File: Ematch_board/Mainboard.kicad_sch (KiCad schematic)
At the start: 72 parts, among them J10 Conn_01x02_Male, J7 Conn_01x06_Female, J8 USB_C_Receptacle_USB2.0, J9 Conn_01x02_Male, Q1 MMDT2222A, Q2 MMDT2222A, U2 LTC4411, U3 RT9025-25GSP, U4 LTC4411, U5 SN65HVD230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

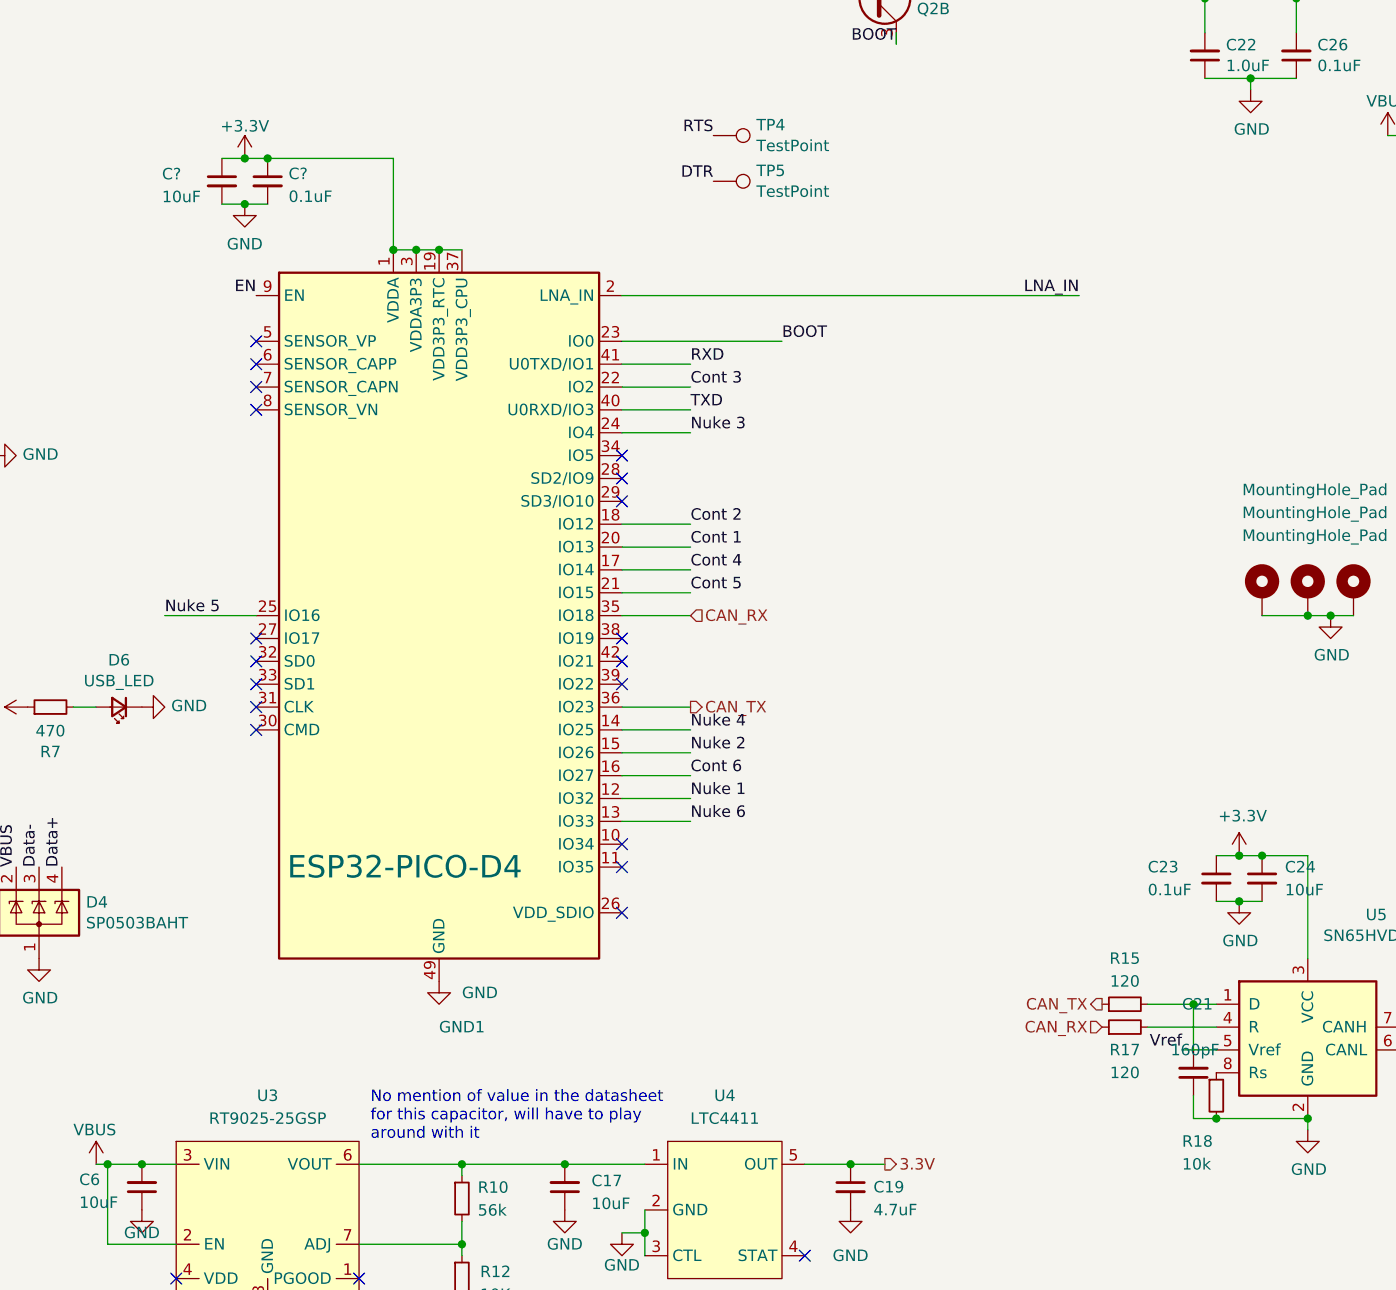
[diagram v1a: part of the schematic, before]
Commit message: removed ground traces
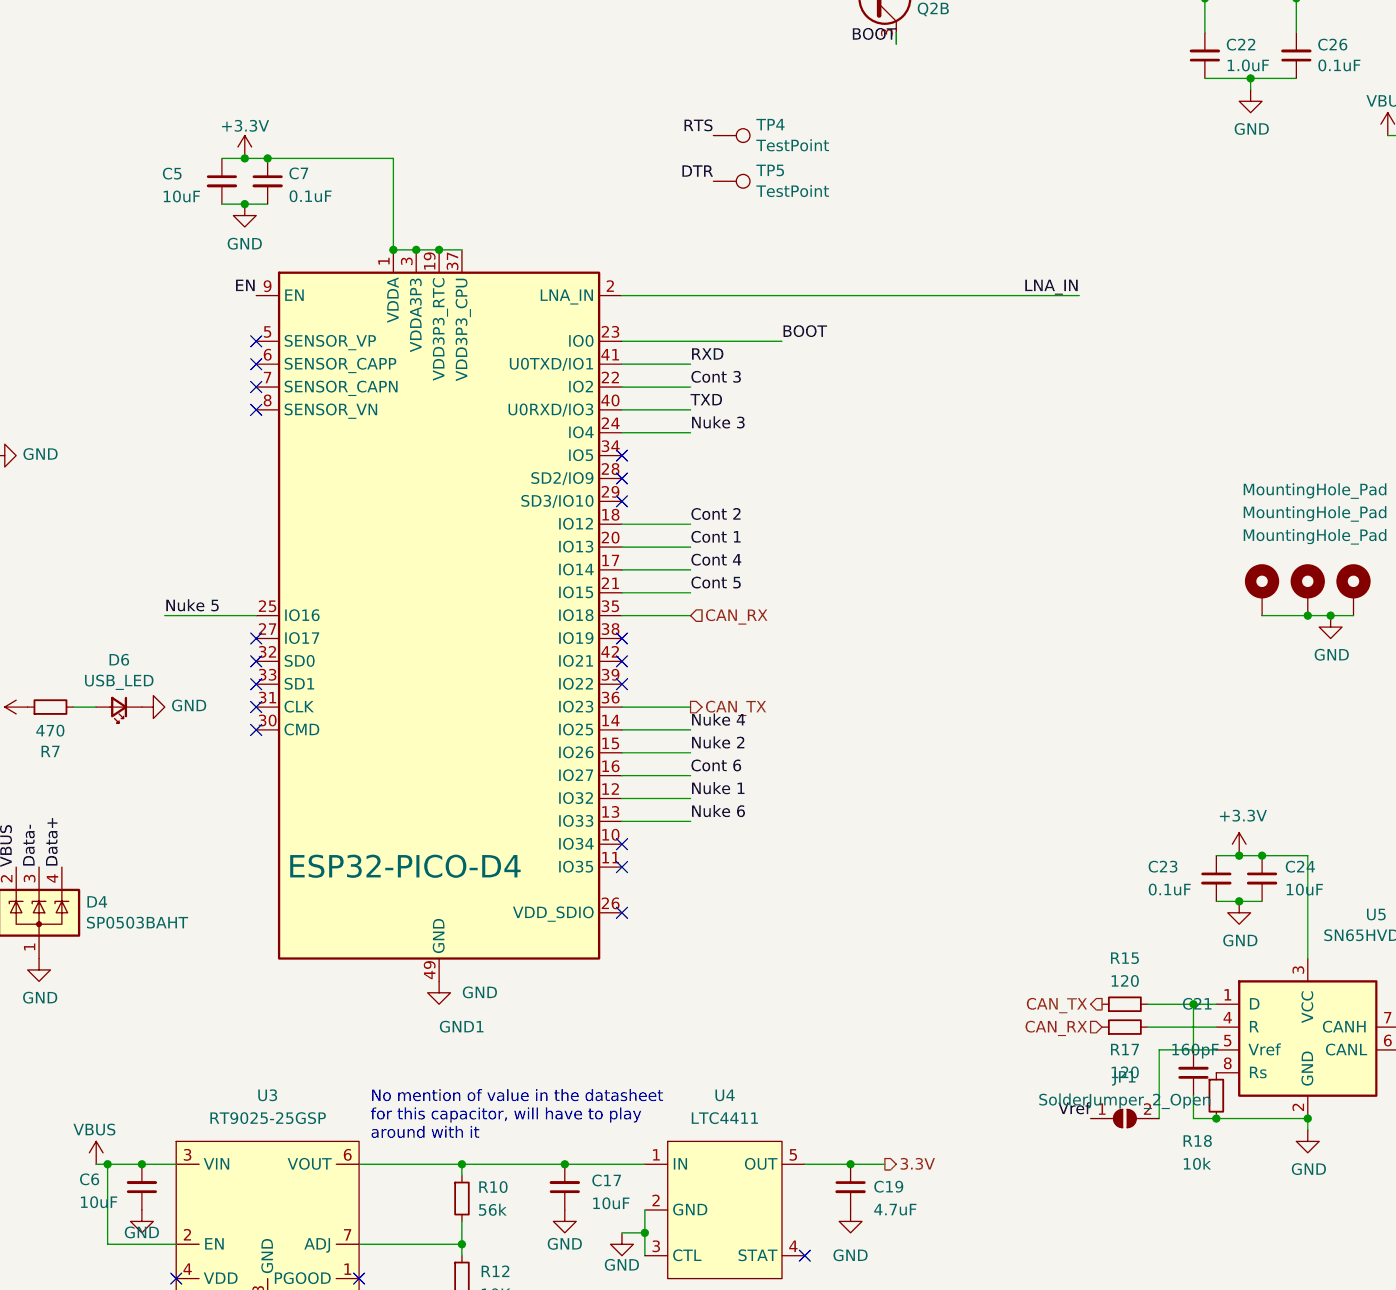
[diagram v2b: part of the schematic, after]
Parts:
- added JP1: SolderJumper_2_Open, Jumper:SolderJumper-2_P1.3mm_Open_RoundedPad1.0x1.5mm, symbol Jumper:SolderJumper_2_Open
- C5, C7: renamed from C?; footprint (none) -> Capacitor_SMD:C_0603_1608Metric
- TP1, TP2, TP3, TP4, TP5: footprint TestPoint:TestPoint_THTPad_1.0x1.0mm_Drill0.5mm -> TestPoint:TestPoint_Pad_D1.0mm
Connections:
- net Vref: now also JP1.1 (A); no longer U5.5 (Vref)
- new net: JP1.2 (B), U5.5 (Vref)
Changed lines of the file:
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@@
     (stroke (width 0) (type default) (color 0 0 0 0))
   )
-  (wire (pts (xy 186.69 154.94) (xy 190.5 154.94))
+  (wire (pts (xy 184.15 154.94) (xy 190.5 154.94))
     (stroke (width 0) (type default) (color 0 0 0 0))
   )
@@
   )
   (wire (pts (xy -12.7 91.44) (xy -5.08 91.44))
+    (stroke (width 0) (type default) (color 0 0 0 0))
+  )
+  (wire (pts (xy 184.15 162.56) (xy 184.15 154.94))
     (stroke (width 0) (type default) (color 0 0 0 0))
   )
@@
     (effects (font (size 1.27 1.27)) (justify right bottom))
   )
+  (label "Vref" (at 176.53 162.56 180)
+    (effects (font (size 1.27 1.27)) (justify right bottom))
+  )
   (label "Data-" (at 200.66 33.02 0)
     (effects (font (size 1.27 1.27)) (justify left bottom))
@@
   (label "Cont 5" (at 132.08 104.14 0)
     (effects (font (size 1.27 1.27)) (justify left bottom))
-  )
-  (label "Vref" (at 186.69 154.94 180)
-    (effects (font (size 1.27 1.27)) (justify right bottom))
   )
   (label "Data-" (at 44.45 95.25 0)
@@
       (effects (font (size 1.27 1.27)) (justify left))
     )
-    (property "Footprint" "TestPoint:TestPoint_THTPad_1.0x1.0mm_Drill0.5mm" (id 2) (at 134.62 63.5 0)
+    (property "Footprint" "TestPoint:TestPoint_Pad_D1.0mm" (id 2) (at 134.62 63.5 0)
       (effects (font (size 1.27 1.27)) hide)
     )
@@
       (effects (font (size 1.27 1.27)) (justify left))
     )
-    (property "Footprint" "TestPoint:TestPoint_THTPad_1.0x1.0mm_Drill0.5mm" (id 2) (at -5.08 106.68 0)
+    (property "Footprint" "TestPoint:TestPoint_Pad_D1.0mm" (id 2) (at -5.08 106.68 0)
       (effects (font (size 1.27 1.27)) hide)
     )
@@
       (effects (font (size 1.27 1.27)) (justify left))
     )
-    (property "Footprint" "TestPoint:TestPoint_THTPad_1.0x1.0mm_Drill0.5mm" (id 2) (at -5.08 101.6 0)
+    (property "Footprint" "TestPoint:TestPoint_Pad_D1.0mm" (id 2) (at -5.08 101.6 0)
       (effects (font (size 1.27 1.27)) hide)
     )
@@
   (symbol (lib_id "power:GND") (at 82.55 60.96 0) (unit 1)
     (in_bom yes) (on_board yes) (fields_autoplaced)
-    (property "Reference" "#PWR?" (id 0) (at 82.55 67.31 0)
+    (property "Reference" "#PWR0114" (id 0) (at 82.55 67.31 0)
       (effects (font (size 1.27 1.27)) hide)
     )
@@
     (pin "2")
   )
+  (symbol (lib_id "Jumper:SolderJumper_2_Open") (at 180.34 162.56 0) (unit 1)
+    (in_bom yes) (on_board yes) (fields_autoplaced)
+    (property "Reference" "JP1" (id 0) (at 180.34 157.9712 0))
+    (property "Value" "SolderJumper_2_Open" (id 1) (at 180.34 160.5081 0))
+    (property "Footprint" "Jumper:SolderJumper-2_P1.3mm_Open_RoundedPad1.0x1.5mm" (id 2) (at 180.34 162.56 0)
+      (effects (font (size 1.27 1.27)) hide)
+    )
+    (property "Datasheet" "~" (id 3) (at 180.34 162.56 0)
+      (effects (font (size 1.27 1.27)) hide)
+    )
+    (pin "1")
+    (pin "2")
+  )
   (symbol (lib_id "Device:LED_Small") (at 68.58 116.84 180) (unit 1)
     (in_bom yes) (on_board yes)
@@
   (symbol (lib_id "Device:C_Small") (at 80.01 58.42 0) (unit 1)
     (in_bom yes) (on_board yes)
-    (property "Reference" "C?" (id 0) (at 73.3516 57.6146 0)
+    (property "Reference" "C5" (id 0) (at 73.3516 57.6146 0)
       (effects (font (size 1.27 1.27)) (justify left))
     )
@@
       (effects (font (size 1.27 1.27)) (justify left))
     )
-    (property "Footprint" "" (id 2) (at 80.01 58.42 0)
+    (property "Footprint" "Capacitor_SMD:C_0603_1608Metric" (id 2) (at 80.01 58.42 0)
       (effects (font (size 1.27 1.27)) hide)
     )
@@
   (symbol (lib_id "Device:C_Small") (at 85.09 58.42 0) (unit 1)
     (in_bom yes) (on_board yes) (fields_autoplaced)
-    (property "Reference" "C?" (id 0) (at 87.4141 57.5916 0)
+    (property "Reference" "C7" (id 0) (at 87.4141 57.5916 0)
       (effects (font (size 1.27 1.27)) (justify left))
     )
@@
       (effects (font (size 1.27 1.27)) (justify left))
     )
-    (property "Footprint" "" (id 2) (at 85.09 58.42 0)
+    (property "Footprint" "Capacitor_SMD:C_0603_1608Metric" (id 2) (at 85.09 58.42 0)
       (effects (font (size 1.27 1.27)) hide)
     )
@@
       (effects (font (size 1.27 1.27)) (justify left))
     )
-    (property "Footprint" "TestPoint:TestPoint_THTPad_1.0x1.0mm_Drill0.5mm" (id 2) (at 134.62 58.42 0)
+    (property "Footprint" "TestPoint:TestPoint_Pad_D1.0mm" (id 2) (at 134.62 58.42 0)
       (effects (font (size 1.27 1.27)) hide)
     )
@@
   (symbol (lib_id "power:+3.3V") (at 82.55 55.88 0) (unit 1)
     (in_bom yes) (on_board yes) (fields_autoplaced)
-    (property "Reference" "#PWR?" (id 0) (at 82.55 59.69 0)
+    (property "Reference" "#PWR0115" (id 0) (at 82.55 59.69 0)
       (effects (font (size 1.27 1.27)) hide)
     )
@@
       (effects (font (size 1.27 1.27)) (justify left))
     )
-    (property "Footprint" "TestPoint:TestPoint_THTPad_1.0x1.0mm_Drill0.5mm" (id 2) (at -5.08 96.52 0)
+    (property "Footprint" "TestPoint:TestPoint_Pad_D1.0mm" (id 2) (at -5.08 96.52 0)
       (effects (font (size 1.27 1.27)) hide)
     )
@@
       (reference "#PWR0113") (unit 1) (value "VBUS") (footprint "")
     )
+    (path "/36f6ae3c-ef64-4b29-8151-a955bfe5c8b5"
+      (reference "#PWR0114") (unit 1) (value "GND") (footprint "")
+    )
+    (path "/e3849e21-3723-4744-8c66-4518d9abc271"
+      (reference "#PWR0115") (unit 1) (value "+3.3V") (footprint "")
+    )
     (path "/8d4d894f-79ee-44de-ab8c-e56cfae62d61"
       (reference "#PWR0116") (unit 1) (value "GND") (footprint "")
@@
       (reference "#PWR0165") (unit 1) (value "GND") (footprint "")
     )
-    (path "/36f6ae3c-ef64-4b29-8151-a955bfe5c8b5"
-      (reference "#PWR?") (unit 1) (value "GND") (footprint "")
-    )
-    (path "/e3849e21-3723-4744-8c66-4518d9abc271"
-      (reference "#PWR?") (unit 1) (value "+3.3V") (footprint "")
-    )
     (path "/0a7b15e5-0143-46cb-ba4d-79b927deec53"
       (reference "ANT1") (unit 1) (value "AMCA31-2R450G-S1F-T3") (footprint "iclr:ANT_AMCA31-2R450G-S1F-T3")
@@
       (reference "C4") (unit 1) (value "4.7uF") (footprint "Capacitor_SMD:C_0603_1608Metric")
     )
+    (path "/502ceb05-80c8-48a6-b40a-921ed2d990a1"
+      (reference "C5") (unit 1) (value "10uF") (footprint "Capacitor_SMD:C_0603_1608Metric")
+    )
     (path "/09e160e9-c302-4f99-8023-5db67f6e253f"
       (reference "C6") (unit 1) (value "10uF") (footprint "Capacitor_SMD:C_0603_1608Metric")
     )
+    (path "/a9bb760d-8f39-4ddc-b3eb-2c9f4b8ac082"
+      (reference "C7") (unit 1) (value "0.1uF") (footprint "Capacitor_SMD:C_0603_1608Metric")
+    )
     (path "/01e8f8ae-dce9-4289-ad51-61b0643fb392"
       (reference "C16") (unit 1) (value "33pF") (footprint "Capacitor_SMD:C_0603_1608Metric")
@@
       (reference "C29") (unit 1) (value "C_Small") (footprint "Capacitor_SMD:C_0603_1608Metric")
     )
-    (path "/502ceb05-80c8-48a6-b40a-921ed2d990a1"
-      (reference "C?") (unit 1) (value "10uF") (footprint "")
-    )
-    (path "/a9bb760d-8f39-4ddc-b3eb-2c9f4b8ac082"
-      (reference "C?") (unit 1) (value "0.1uF") (footprint "")
-    )
     (path "/dfb2924b-88e7-4ec5-ace2-e873866fe72c"
       (reference "D1") (unit 1) (value "RX_LED") (footprint "LED_SMD:LED_0603_1608Metric")
@@
       (reference "J10") (unit 1) (value "Conn_01x02_Male") (footprint "Connector_PinHeader_2.54mm:PinHeader_1x02_P2.54mm_Vertical")
     )
+    (path "/3ff4471a-d9da-4126-af01-ea9a764303aa"
+      (reference "JP1") (unit 1) (value "SolderJumper_2_Open") (footprint "Jumper:SolderJumper-2_P1.3mm_Open_RoundedPad1.0x1.5mm")
+    )
     (path "/f1bd5482-3597-4351-8d27-f49c0b73b401"
       (reference "L1") (unit 1) (value "LQG15WZ1N8B02D") (footprint "Inductor_SMD:L_0603_1608Metric_Pad1.05x0.95mm_HandSolder")
@@
     )
     (path "/eeab19a5-eda8-4925-9d02-4935988d1d34"
-      (reference "TP1") (unit 1) (value "TestPoint") (footprint "TestPoint:TestPoint_THTPad_1.0x1.0mm_Drill0.5mm")
+      (reference "TP1") (unit 1) (value "TestPoint") (footprint "TestPoint:TestPoint_Pad_D1.0mm")
     )
     (path "/2163dbd0-9c20-4f43-b9c8-b7932544841e"
-      (reference "TP2") (unit 1) (value "TestPoint") (footprint "TestPoint:TestPoint_THTPad_1.0x1.0mm_Drill0.5mm")
+      (reference "TP2") (unit 1) (value "TestPoint") (footprint "TestPoint:TestPoint_Pad_D1.0mm")
     )
     (path "/0f48419a-c2c8-4aa8-97b7-71e3f2aec018"
-      (reference "TP3") (unit 1) (value "TestPoint") (footprint "TestPoint:TestPoint_THTPad_1.0x1.0mm_Drill0.5mm")
+      (reference "TP3") (unit 1) (value "TestPoint") (footprint "TestPoint:TestPoint_Pad_D1.0mm")
     )
     (path "/ab897d29-2412-46e4-9faf-1bb378719f13"
-      (reference "TP4") (unit 1) (value "TestPoint") (footprint "TestPoint:TestPoint_THTPad_1.0x1.0mm_Drill0.5mm")
+      (reference "TP4") (unit 1) (value "TestPoint") (footprint "TestPoint:TestPoint_Pad_D1.0mm")
     )
     (path "/0d2336aa-db63-4999-80e3-c0d76afae3ce"
-      (reference "TP5") (unit 1) (value "TestPoint") (footprint "TestPoint:TestPoint_THTPad_1.0x1.0mm_Drill0.5mm")
+      (reference "TP5") (unit 1) (value "TestPoint") (footprint "TestPoint:TestPoint_Pad_D1.0mm")
     )
     (path "/00000000-0000-0000-0000-000061c80f8f/f8d3e818-1bd3-47e9-8c88-fecde07281d8"
